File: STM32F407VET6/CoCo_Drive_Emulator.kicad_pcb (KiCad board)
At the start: 2 copper layers, 71.5 x 94.1 mm, 14 parts, among them P1 CoCo_Slot, SW1 PB_Next, SW2 PB_Previous, U1 STM32F407VET6_DevBoard

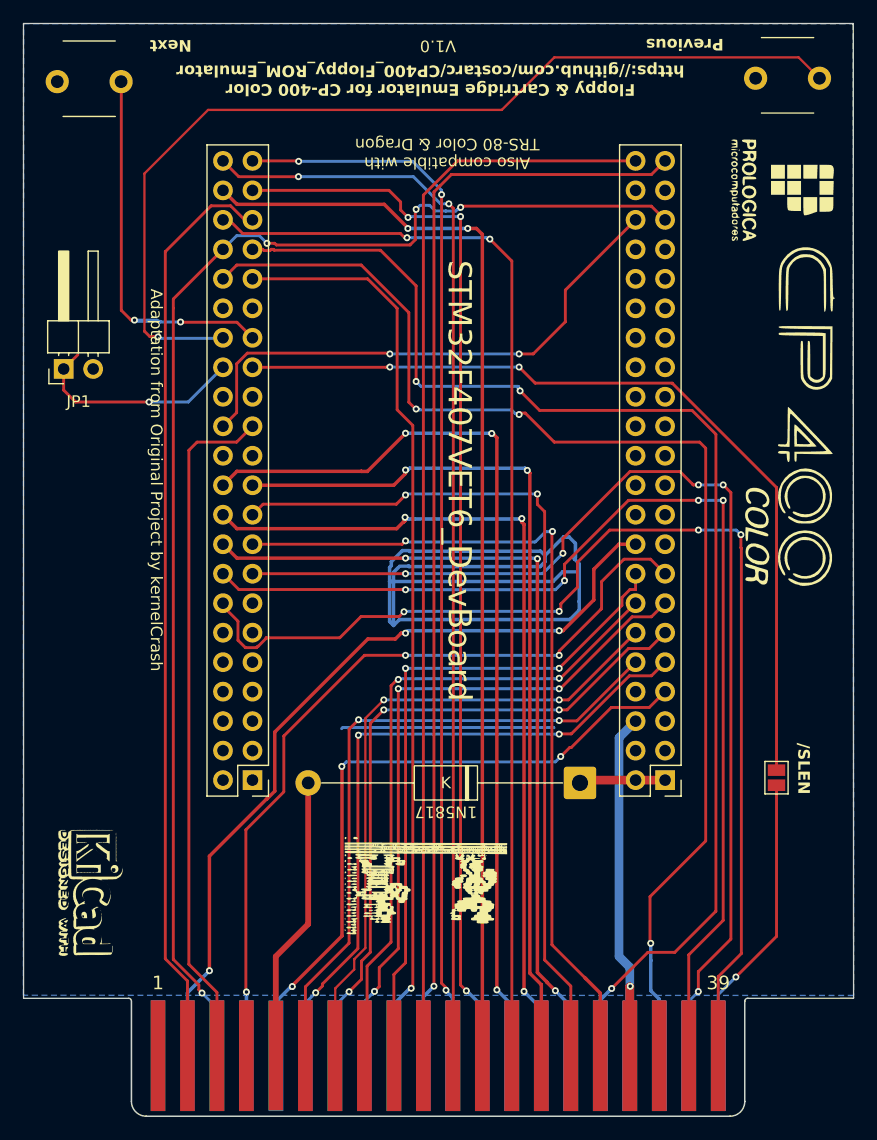
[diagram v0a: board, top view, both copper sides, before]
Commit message: Added header for display
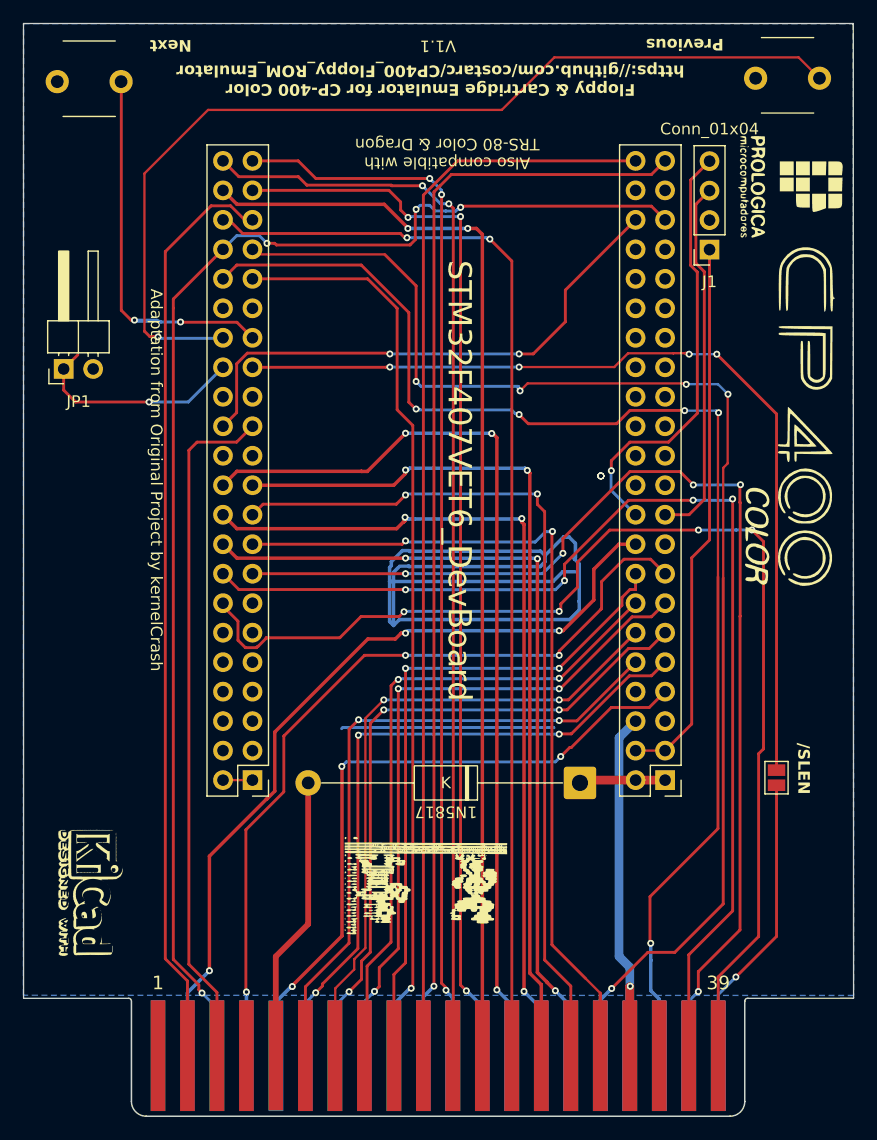
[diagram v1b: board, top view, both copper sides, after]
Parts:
- added J1: Conn_01x04, Connector_PinSocket_2.54mm:PinSocket_1x04_P2.54mm_Vertical, F.Cu at (111.0, 56.7)
- moved G*** 0.81 mm to (118.0, 51.3)
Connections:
- U1 pad 3V3: unconnected-(U1-Pad3V3)_3 -> +3.3V
- U1 pad PA8: unconnected-(U1-PadPA8) -> I2C3_SCL
- U1 pad PC9: unconnected-(U1-PadPC9) -> I2C3_SDA
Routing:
- net +3.3V: track 0.00 -> 49.8 mm
- net I2C3_SDA: track 0.00 -> 37.2 mm, vias 0 -> 1
- net I2C3_SCL: track 0.00 -> 31.3 mm
- net Net-(JP2-A): track 73.8 -> 78.5 mm, vias 2 -> 4
- net /SCS: track 107.9 -> 112.3 mm, vias 3 -> 5
- net /CTS: track 110.6 -> 114.6 mm, vias 3 -> 5
- net PE15: track 99.0 -> 101.4 mm
- net PE14: track 96.5 -> 98.1 mm
- net PE13: track 96.7 -> 98.1 mm
- net GND: vias 1 -> 5
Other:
- board text added: "V1.1"
- board text removed: "V1.0"
